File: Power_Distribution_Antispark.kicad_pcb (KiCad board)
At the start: 2 copper layers, 119 parts, among them J1 STM Signal Conn, J10 CSense12V_2 Conn, J11 CSense12V_3 Conn, J2 +48V Battery Conn, J3 Motor Conn, J4 CSense3V3STM Conn, J5 CSense3V3_2 Conn, J6 CSense5V_1 Conn, J7 CSense5V_2 Conn, J8 CSense5V_3 Conn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

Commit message: component layout
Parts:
- added TP1: TestPoint, TestPoint:TestPoint_Pad_D1.0mm, F.Cu at (158.9, 113.8)
- added TP10: TestPoint, TestPoint:TestPoint_Pad_D1.0mm, F.Cu at (141.0, 121.5)
- added TP11: TestPoint, TestPoint:TestPoint_Pad_D1.0mm, F.Cu at (158.3, 103.7)
- added TP12: TestPoint, TestPoint:TestPoint_Pad_D1.0mm, F.Cu at (158.4, 117.1)
- added TP2: TestPoint, TestPoint:TestPoint_Pad_D1.0mm, F.Cu at (133.8, 100.3)
- added TP3: TestPoint, TestPoint:TestPoint_Pad_D1.0mm, F.Cu at (130.9, 113.7)
- added TP4: TestPoint, TestPoint:TestPoint_Pad_D1.0mm, F.Cu at (108.4, 107.3)
- added TP5: TestPoint, TestPoint:TestPoint_Pad_D1.0mm, F.Cu at (164.2, 96.2)
- added TP6: TestPoint, TestPoint:TestPoint_Pad_D1.0mm, F.Cu at (170.6, 97.5)
- added TP7: TestPoint, TestPoint:TestPoint_Pad_D1.0mm, F.Cu at (128.6, 69.2)
- added TP8: TestPoint, TestPoint:TestPoint_Pad_D1.0mm, F.Cu at (123.6, 111.0)
- added TP9: TestPoint, TestPoint:TestPoint_Pad_D1.0mm, F.Cu at (113.9, 113.4)
- moved F1 153.8 mm to (164.2, 87.3)
- moved D7 149.8 mm to (171.2, 86.9)
- moved J2 146.1 mm to (167.8, 79.7)
- moved Q2 120.6 mm to (133.9, 107.9), turned to 0 degrees
- moved J1 106.9 mm to (151.2, 120.8), turned to 180 degrees
- moved H2 104.4 mm to (107.7, 120.7), turned to 90 degrees
- moved J9 103.2 mm to (125.2, 121.4), turned to 180 degrees
- moved R44 99.3 mm to (125.1, 117.2)
- moved R2 95.1 mm to (132.2, 75.1)
- moved U12 93.1 mm to (125.1, 114.2)
- moved C29 92.6 mm to (128.1, 113.7), turned to -90 degrees
- moved R4 92.1 mm to (119.6, 71.9), turned to 90 degrees
- moved R1 92.0 mm to (132.2, 77.0)
- moved U14 91.6 mm to (143.6, 70.5), turned to 180 degrees
- moved Q1 89.6 mm to (127.5, 72.6), turned to 90 degrees
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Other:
- board text added: "12V"
- board text added: "12V Conn"

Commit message: layout changes
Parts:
- moved TP11 19.5 mm to (144.2, 117.2)
- moved C21 16.6 mm to (147.2, 99.2), turned to 90 degrees
- moved R36 14.7 mm to (145.2, 99.2), turned to -90 degrees
- moved C17 14.0 mm to (144.8, 109.5), turned to 180 degrees
- moved TP2 12.8 mm to (146.5, 102.2)
- moved L1 11.2 mm to (132.5, 99.2), turned to -90 degrees
- moved R33 9.39 mm to (124.0, 83.5)
- moved D10 9.16 mm to (144.0, 106.0), turned to 180 degrees
- moved L2 9.10 mm to (153.5, 107.0), turned to -90 degrees
- moved C19 9.02 mm to (144.8, 112.2), turned to 180 degrees
- moved TP1 8.68 mm to (150.2, 114.5)
- moved D9 8.53 mm to (140.0, 96.8), turned to 0 degrees
- moved R35 6.37 mm to (143.0, 102.2), turned to -90 degrees
- moved R37 6.20 mm to (147.0, 114.5), turned to 0 degrees
- moved C16 4.84 mm to (140.8, 101.5), turned to 90 degrees
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
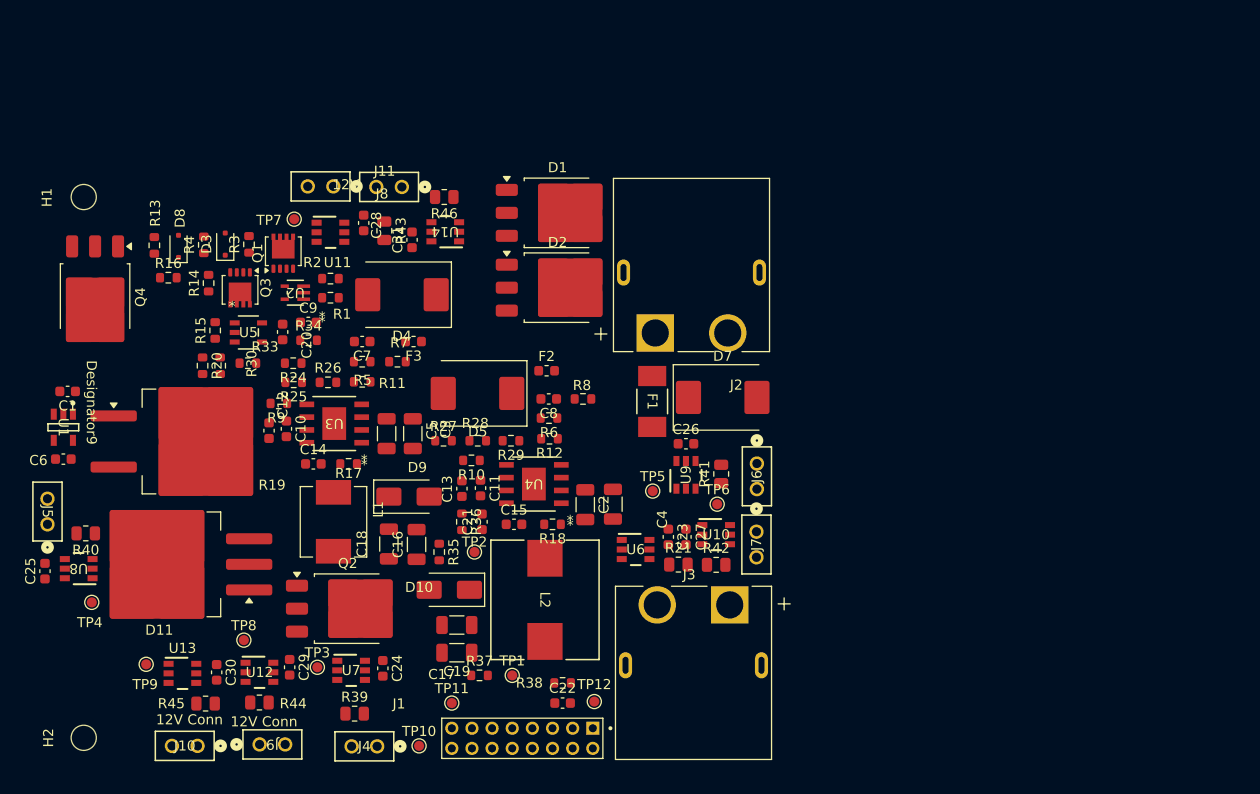
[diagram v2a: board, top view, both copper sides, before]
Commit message: redid layout components
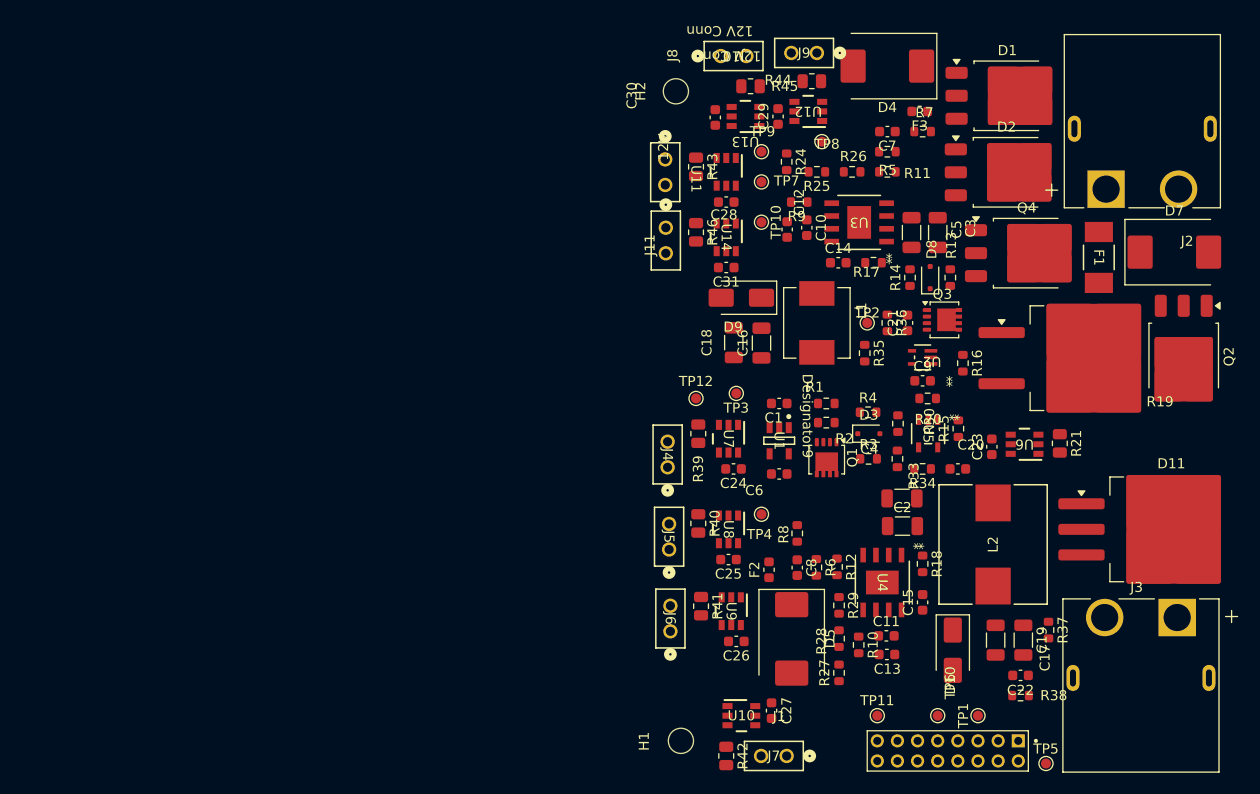
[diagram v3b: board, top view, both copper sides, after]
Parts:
- moved D11 98.0 mm to (214.4, 100.0), turned to 0 degrees
- moved Q4 92.6 mm to (201.3, 72.6), turned to 0 degrees
- moved R19 88.6 mm to (206.5, 83.0)
- moved J9 88.2 mm to (180.5, 52.7), turned to 0 degrees
- moved H2 87.1 mm to (166.5, 56.5)
- moved Q2 86.7 mm to (216.9, 82.8), turned to -90 degrees
- moved J10 86.0 mm to (171.0, 53.0), turned to 180 degrees
- moved R44 82.6 mm to (180.0, 55.5), turned to 180 degrees
- moved R45 81.8 mm to (173.9, 56.0), turned to 0 degrees
- moved H1 80.2 mm to (167.0, 121.0)
- moved TP9 79.5 mm to (175.0, 62.5), turned to 180 degrees
- moved R16 79.4 mm to (195.0, 83.5), turned to -90 degrees
- moved R13 79.1 mm to (193.8, 75.0)
- moved U13 78.6 mm to (173.4, 59.0), turned to 180 degrees
- moved U12 77.9 mm to (179.6, 58.5), turned to 180 degrees
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
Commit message: layout2
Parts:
- moved J10 72.6 mm to (190.5, 122.9), turned to 0 degrees
- moved J9 70.4 mm to (180.3, 123.1), turned to 180 degrees
- moved R45 65.4 mm to (187.5, 120.0)
- moved R44 64.6 mm to (181.5, 120.1), turned to 0 degrees
- moved C30 61.0 mm to (191.0, 116.5), turned to -90 degrees
- moved J11 60.7 mm to (195.1, 123.0), turned to 180 degrees
- moved U13 59.8 mm to (188.0, 117.0), turned to 0 degrees
- moved U12 58.6 mm to (180.9, 117.1), turned to 0 degrees
- moved C29 58.0 mm to (183.9, 116.6), turned to -90 degrees
- moved R46 56.4 mm to (195.6, 120.0), turned to 0 degrees
- moved U14 52.2 mm to (196.1, 117.0), turned to 0 degrees
- moved R42 52.1 mm to (168.5, 70.5), turned to 180 degrees
- moved C31 51.1 mm to (199.1, 117.0), turned to -90 degrees
- moved TP9 50.3 mm to (186.5, 111.5)
- moved J7 46.7 mm to (167.0, 77.0), turned to -90 degrees
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
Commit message: Add files via upload
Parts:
- moved TP6 42.6 mm to (166.9, 65.0)
- moved R21 36.2 mm to (202.1, 123.1)
- moved U6 36.2 mm to (202.1, 119.6)
- moved C23 36.2 mm to (202.2, 116.2)
- moved J5 24.9 mm to (162.4, 102.1), turned to -90 degrees
- moved TP8 23.8 mm to (191.9, 113.2)
- moved TP10 22.5 mm to (172.4, 115.7)
- moved R40 21.7 mm to (165.3, 100.0), turned to -90 degrees
- moved C31 20.0 mm to (179.1, 116.7)
- moved J11 20.0 mm to (175.1, 122.7)
- moved U14 20.0 mm to (176.1, 116.7)
- moved R46 19.6 mm to (176.0, 119.7)
- moved U8 17.9 mm to (168.3, 100.1), turned to -90 degrees
- moved C25 16.1 mm to (168.8, 103.2), turned to 180 degrees
- moved TP5 14.2 mm to (166.5, 109.5)
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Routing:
- added copper zone on In1.Cu, net GND
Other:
- board outline added: 61.5 x 76 mm
- copper layers 2 -> 4
- board text added: "12v"
- board text added: "3v3"
- board text added: "5V"
- board text added: "POWER IN"
- board text added: "POWER OUT"
- board text removed: "12V Conn"

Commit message: most traces
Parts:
- moved TP6 52.0 mm to (169.6, 116.9)
- moved TP5 33.6 mm to (169.0, 76.0)
- moved TP11 32.5 mm to (198.9, 121.1)
- moved J7 8.01 mm to (162.0, 64.0), turned to 90 degrees
- moved C27 7.72 mm to (171.0, 66.0), turned to 90 degrees
- moved C8 5.10 mm to (181.7, 96.0), turned to 90 degrees
- moved R6 5.00 mm to (183.5, 96.0), turned to 90 degrees
- moved C30 4.31 mm to (183.5, 114.0), turned to 180 degrees
- moved R8 4.25 mm to (180.2, 98.5), turned to 180 degrees
- moved U10 3.94 mm to (168.0, 65.5)
- moved C28 3.89 mm to (172.0, 60.0), turned to 0 degrees
- moved C25 3.72 mm to (171.5, 100.7), turned to 90 degrees
- moved C31 3.68 mm to (176.6, 114.0), turned to 180 degrees
- moved C29 3.62 mm to (194.4, 113.7), turned to 180 degrees
- moved C26 3.55 mm to (171.0, 80.0), turned to 90 degrees
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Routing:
- net GND: track 0.00 -> 140.9 mm, vias 0 -> 12
- net /C_Sense_5V_3: track 0.00 -> 71.5 mm, vias 0 -> 2
- net /V_S_5V_Output: track 0.00 -> 64.2 mm, vias 0 -> 2
- net /C_Sense_5V_2: track 0.00 -> 60.4 mm, vias 0 -> 2
- net Net-(D2-K): track 0.00 -> 55.8 mm, vias 0 -> 2
- net +5V: track 0.00 -> 49.4 mm, vias 0 -> 8
- net Net-(D3-K): track 0.00 -> 45.6 mm, vias 0 -> 4
- net /PreCharge_Sense: track 0.00 -> 43.2 mm, vias 0 -> 2
- net /C_Sense_3V3_STM: track 0.00 -> 41.8 mm, vias 0 -> 1
- net /C_Sense_5V_1: track 0.00 -> 38.4 mm, vias 0 -> 1
- net /MotorConn: track 0.00 -> 36.2 mm
- net Net-(D11-A): track 0.00 -> 31.8 mm
- net +3V3: track 0.00 -> 31.1 mm, vias 0 -> 3
- net Net-(Q4-D): track 0.00 -> 30.8 mm, vias 0 -> 4
- net /C_Sense_12V_1: track 0.00 -> 30.6 mm, vias 0 -> 2
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- added copper zone on F.Cu, net +12V
- added copper zone on In2.Cu, net +12V
- added copper zone on In2.Cu, net +3V3
- added copper zone on F.Cu, net +48V
- added copper zone on In2.Cu, net +48V
- added copper zone on F.Cu, net +5V
- added copper zone on In2.Cu, net +5V
- added copper zone on F.Cu, net GND

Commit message: all traces
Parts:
- moved TP1 3.48 mm to (201.3, 114.3)
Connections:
- J1 pad 4: /C_Sense_12V_1 -> /V_S_12V_Output
- J1 pad 5: /V_S_12V_Output -> GND
- J1 pad 6: GND -> /C_Sense_12V_1
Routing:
- net +5V: track 49.4 -> 111.3 mm, vias 8 -> 10
- net /V_S_12V_Output: track 0.00 -> 43.8 mm, vias 0 -> 2
- net GND: track 140.9 -> 156.2 mm, vias 12 -> 16
- net /C_Sense_12V_1: track 30.6 -> 30.0 mm

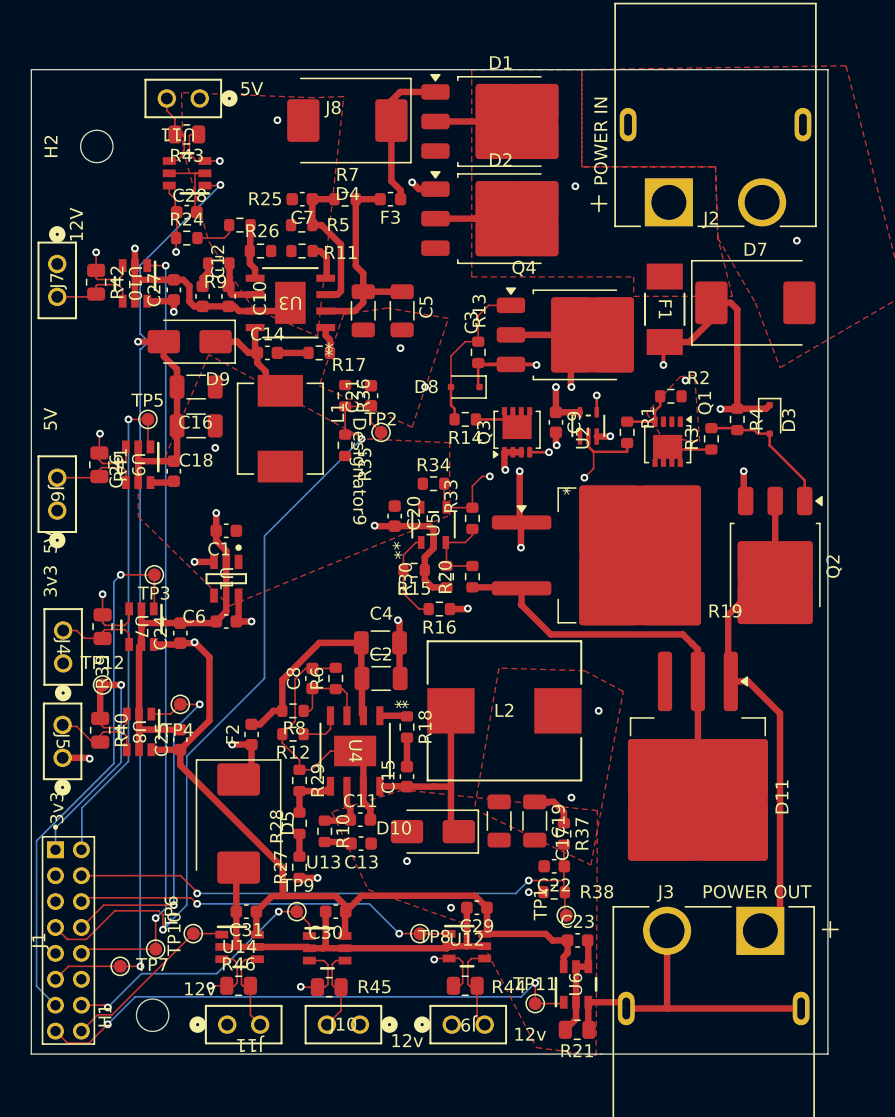
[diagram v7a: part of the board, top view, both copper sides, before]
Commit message: updated traces
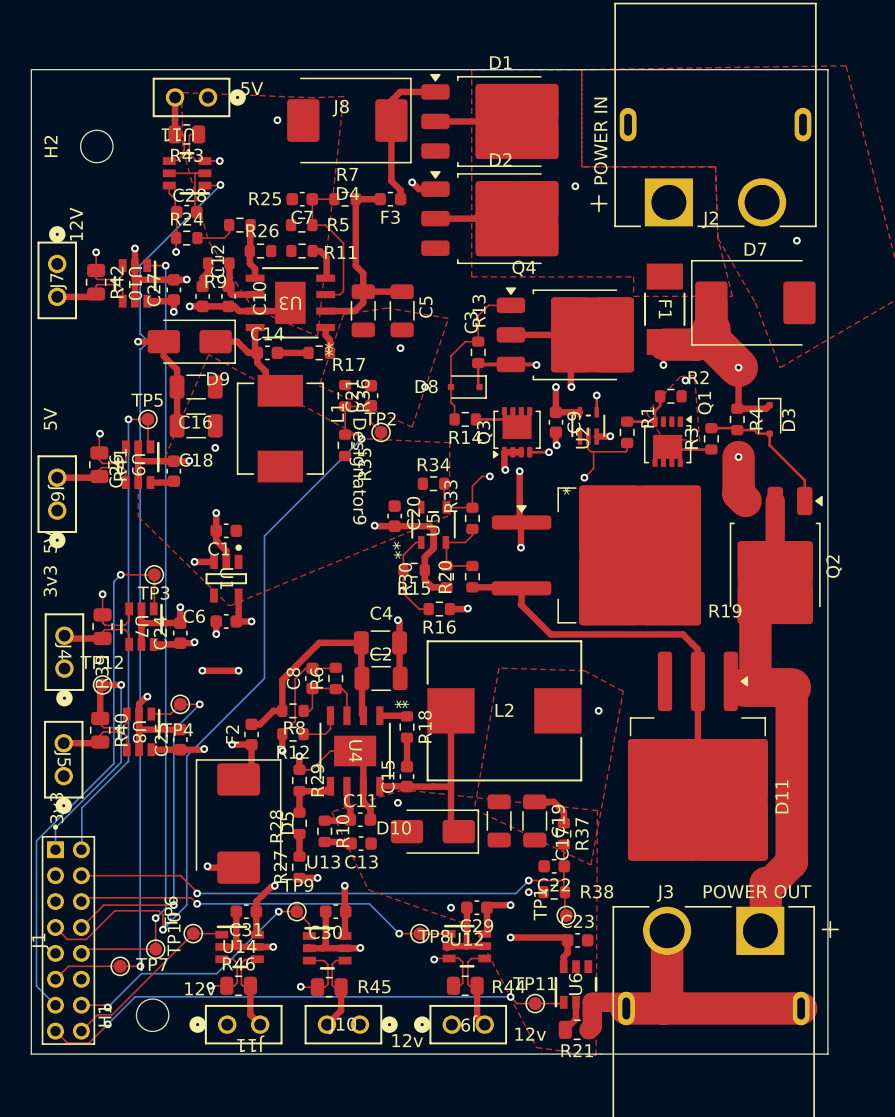
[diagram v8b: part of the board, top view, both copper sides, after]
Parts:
- moved J5 1.42 mm to (162.5, 103.5)
- moved J8 0.64 mm to (173.6, 51.1)
- moved J4 0.41 mm to (162.6, 95.2)
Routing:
- net GND: track 156.2 -> 124.9 mm, vias 16 -> 26
- net +5V: track 111.3 -> 122.2 mm, vias 10 -> 15
- net +3V3: track 31.1 -> 33.9 mm, vias 3 -> 5
- net /PreCharge_Sense: track 43.2 -> 41.3 mm
- net /MotorConn: track 36.2 -> 37.3 mm
- net Net-(D3-K): track 45.6 -> 46.2 mm
- net +12V: vias 6 -> 5
